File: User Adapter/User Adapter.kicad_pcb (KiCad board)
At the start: 2 copper layers, 88.9 x 27.9 mm, 20 parts, among them J1 OHIS_8p8c_Shield, J2 Headphones, J3 Microphone, J4 PTT, J5 Dynamic Mic Bypass, J6 HP or CTIA, Q1 2N3904, SW1 SW_Push

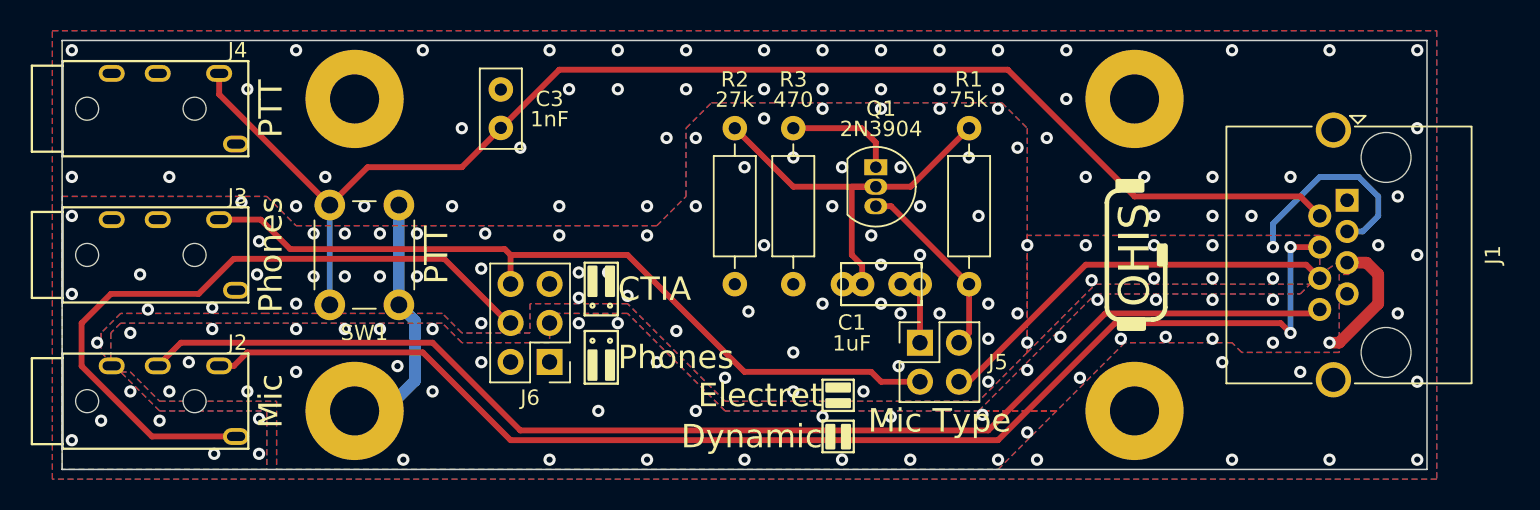
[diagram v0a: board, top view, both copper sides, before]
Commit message: https://github.com/open-headset-interconnect-standard/ohis/issues/14 v1.0a as ordered 2023-10-05.
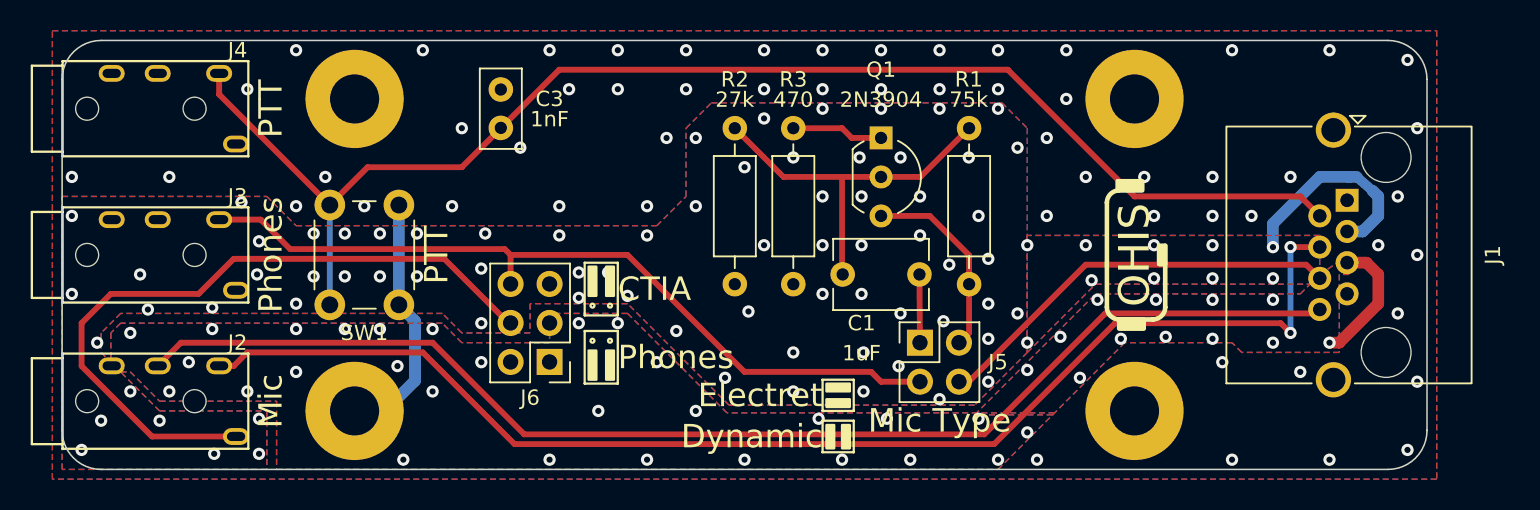
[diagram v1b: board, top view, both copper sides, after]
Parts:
- removed C2: 1uF, Capacitor_THT:C_Disc_D5.0mm_W2.5mm_P5.00mm
- added BOM1: .1" Jumper, Libraries:BOM_Item, F.Cu at (196.3, 67.4)
- added BOM10: M3 6mm SS screw, Libraries:BOM_Item, F.Cu at (196.0, 88.4)
- added BOM11: M3 6mm SS screw, Libraries:BOM_Item, F.Cu at (197.5, 85.4)
- added BOM12: M3 6mm SS screw, Libraries:BOM_Item, F.Cu at (197.5, 86.9)
- added BOM13: M3 10mm SS screw, Libraries:BOM_Item, F.Cu at (197.5, 88.4)
- added BOM14: M3 10mm SS screw, Libraries:BOM_Item, F.Cu at (194.1, 89.7)
- added BOM15: M3 10mm SS screw, Libraries:BOM_Item, F.Cu at (194.1, 91.2)
- added BOM16: M3 10mm SS screw, Libraries:BOM_Item, F.Cu at (195.6, 89.7)
- added BOM17: Main Board, Libraries:BOM_Item, F.Cu at (195.3, 79.5)
- added BOM18: Top Board, Libraries:BOM_Item, F.Cu at (195.3, 81.0)
- added BOM19: Bottom Board, Libraries:BOM_Item, F.Cu at (195.6, 91.2)
- added BOM2: .1" Jumper, Libraries:BOM_Item, F.Cu at (196.3, 68.9)
- added BOM20: M3 3mm ABS standoff, Libraries:BOM_Item, F.Cu at (197.1, 89.7)
- added BOM21: M3 3mm ABS standoff, Libraries:BOM_Item, F.Cu at (197.1, 91.2)
- added BOM22: M3 3mm ABS standoff, Libraries:BOM_Item, F.Cu at (198.6, 89.7)
- added BOM23: M3 3mm ABS standoff, Libraries:BOM_Item, F.Cu at (198.6, 91.2)
- added BOM3: .1" Jumper, Libraries:BOM_Item, F.Cu at (196.3, 70.4)
- added BOM4: .1" Jumper, Libraries:BOM_Item, F.Cu at (196.3, 71.9)
- added BOM5: M3 14mm brass standoff, Libraries:BOM_Item, F.Cu at (194.5, 85.4)
- added BOM6: M3 14mm brass standoff, Libraries:BOM_Item, F.Cu at (194.5, 86.9)
- added BOM7: M3 14mm brass standoff, Libraries:BOM_Item, F.Cu at (194.5, 88.4)
- added BOM8: M3 14mm brass standoff, Libraries:BOM_Item, F.Cu at (196.0, 85.4)
- added BOM9: M3 6mm SS screw, Libraries:BOM_Item, F.Cu at (196.0, 86.9)
- C1: footprint Capacitor_THT:C_Disc_D5.0mm_W2.5mm_P2.50mm -> Capacitor_THT:C_Disc_D6.0mm_W4.4mm_P5.00mm
- Q1: footprint Package_TO_SOT_THT:TO-92_Inline -> Package_TO_SOT_THT:TO-92_Inline_Wide
- SW1: value SW_Push -> PTT
- moved Q1 1.94 mm to (154.9, 68.6)
- moved C1 1.38 mm to (157.4, 77.5)
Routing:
- net Net-(Q1-B): track 27.9 -> 24.9 mm
- net Net-(Q1-E): track 7.37 -> 5.98 mm
- net Net-(J5-Pin_2): track 12.3 -> 12.8 mm
- net Mic-: vias 79 -> 84
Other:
- outline, holes or cut-outs redrawn

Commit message: Fixed silkscreen art, added trimpot. #1
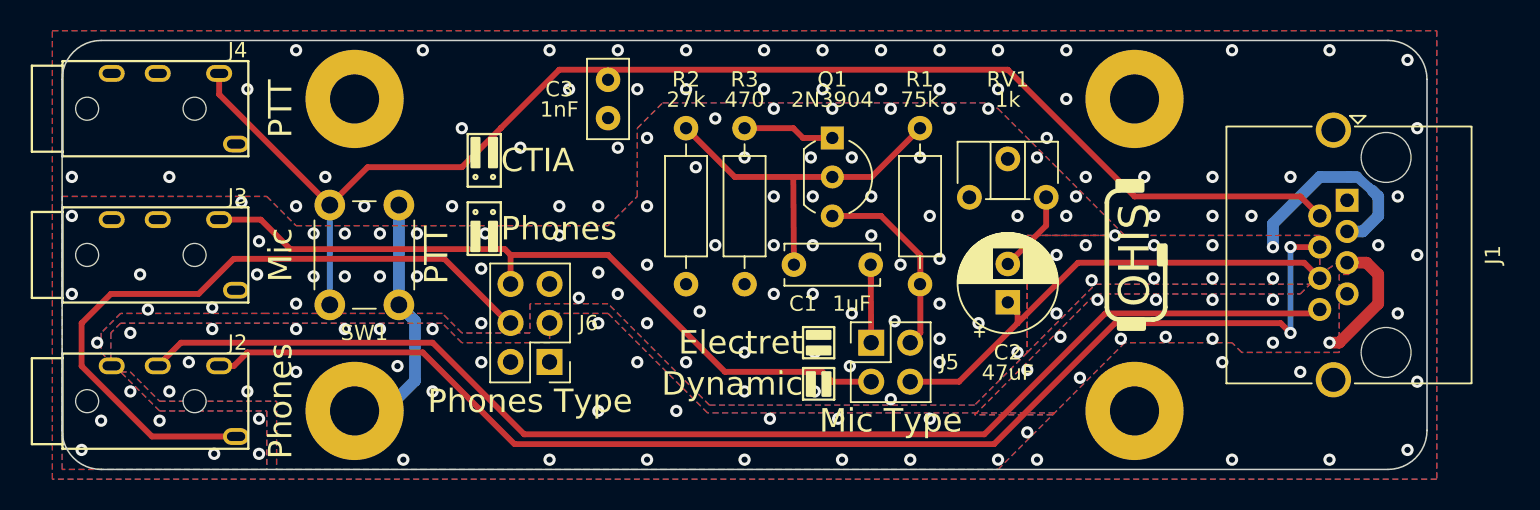
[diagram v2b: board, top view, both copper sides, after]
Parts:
- added C2: 47uF, Capacitor_THT:CP_Radial_D6.3mm_P2.50mm, F.Cu at (163.2, 79.3)
- added RV1: 1k, Potentiometer_THT:Potentiometer_Piher_PT-6-H_Horizontal, F.Cu at (160.7, 72.4)
- C1: footprint Capacitor_THT:C_Disc_D6.0mm_W4.4mm_P5.00mm -> Capacitor_THT:C_Disc_D6.0mm_W2.5mm_P5.00mm
- moved C3 7.23 mm to (137.2, 67.3), turned to 90 degrees
- moved C1 3.24 mm to (154.3, 76.8)
- moved R1 3.20 mm to (157.5, 78.1)
- moved Q1 3.18 mm to (151.8, 68.6)
- moved J5 3.17 mm to (154.3, 81.9)
- moved R2 3.17 mm to (142.2, 67.9)
- moved R3 3.17 mm to (146.1, 67.9)
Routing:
- net Net-(C2-Pad2): track 0.00 -> 5.38 mm
- net Mic+: track 27.0 -> 31.9 mm
- net Mic+ 3.5: track 51.9 -> 48.7 mm
- net Net-(Q1-B): track 24.9 -> 23.6 mm
- net Net-(J5-Pin_1): track 5.08 -> 6.35 mm
- net Mic-: vias 84 -> 91
- net HP:G: vias 41 -> 40
- net GND: vias 56 -> 55
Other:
- board text added: "1k"
- board text added: "47uF"
- board text added: "JLCJLCJLCJLC"
- board text added: "OHIS Open Source User Adapter v1.1a 2024 CC-BY OHIS Working Group"
- board text added: "Phones Type"
- board text removed: "OHIS Open Source User Adapter 2023 CC-BY OHIS Working Group"

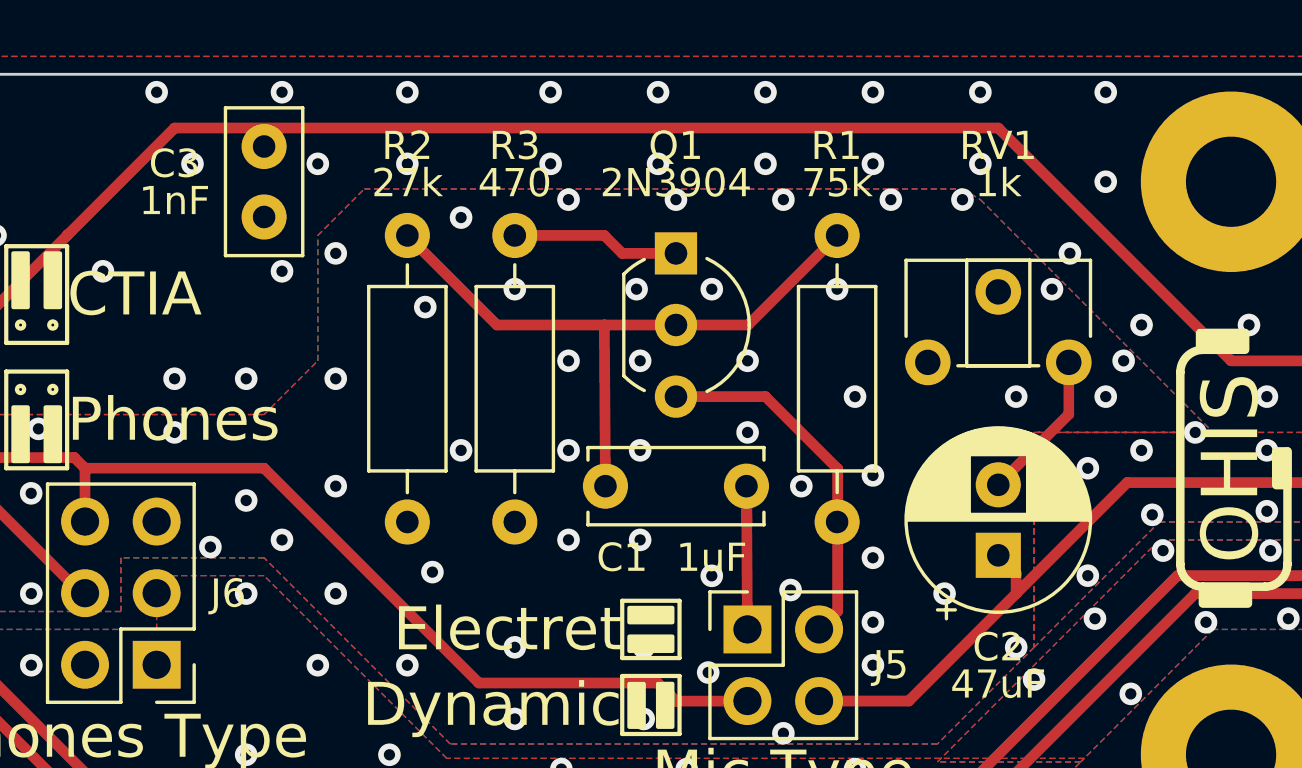
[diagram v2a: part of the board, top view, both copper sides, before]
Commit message: Very minor changes to the silkscreen when ordering. AS ORDERED prototypes v1.1
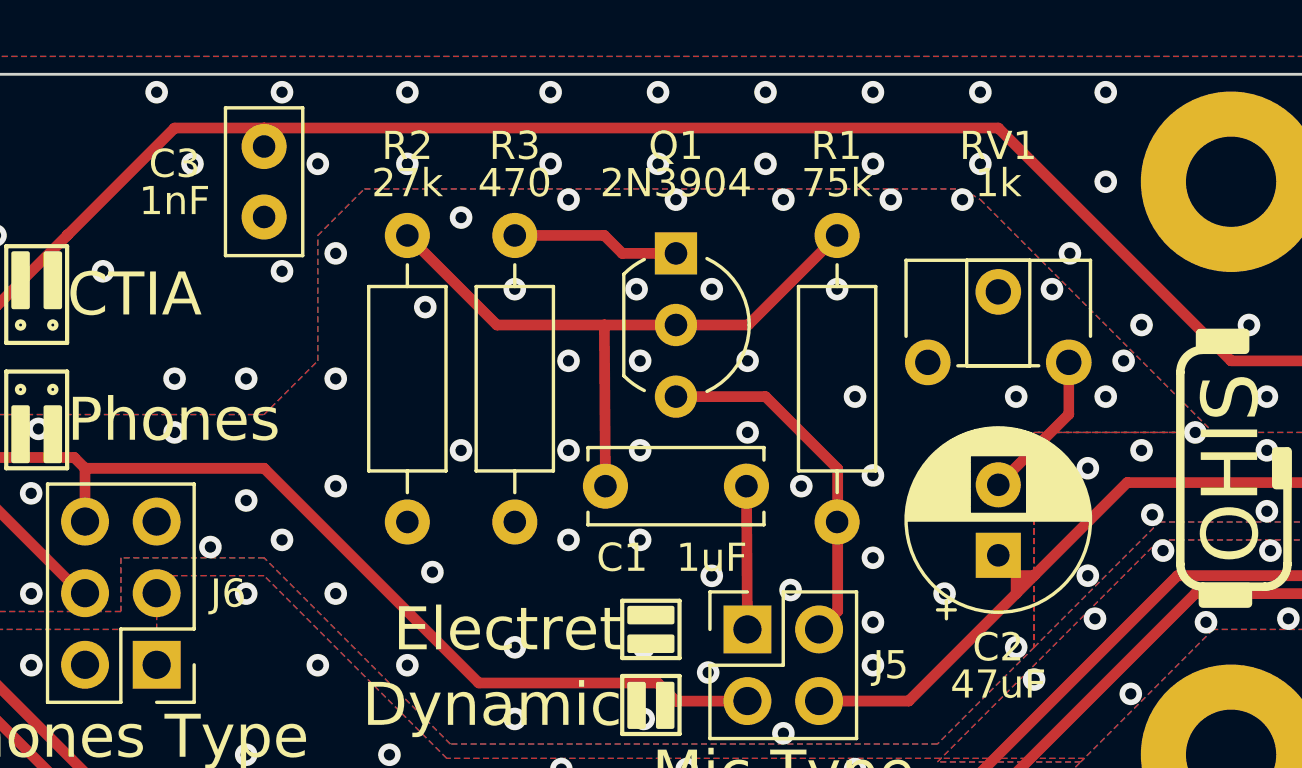
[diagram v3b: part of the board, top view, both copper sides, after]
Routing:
- net Mic+: track 31.9 -> 33.5 mm
- net Net-(J5-Pin_1): track 6.35 -> 5.08 mm
- net PTT: track 90.1 -> 90.8 mm
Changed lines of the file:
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@@
     (effects (font (size 1.27 1.27) (thickness 0.1905)) (justify left mirror))
   )
-  (gr_text "OHIS Open Source User Adapter v1.1a\n2024 CC-BY OHIS Working Group" (at 166.37 66.675) (layer "B.SilkS")
-    (effects (font (size 1.27 1.27) (thickness 0.1905)) (justify left bottom mirror))
-  )
-  (gr_text "https://github.com/open-headset-interconnect-standard/user-adapter" (at 180.34 76.581) (layer "B.SilkS")
+  (gr_text "OHIS Open Source User Adapter v1.1a\n2024 CC-BY OHIS Working Group" (at 167.64 66.675) (layer "B.SilkS")
+    (effects (font (size 1.27 1.016) (thickness 0.1905)) (justify left bottom mirror))
+  )
+  (gr_text "https://github.com/open-headset-interconnect-standard/user-adapter" (at 180.34 75.819) (layer "B.SilkS")
     (effects (font (size 1 1) (thickness 0.15)) (justify left bottom mirror))
   )
@@
   (segment (start 171.45 72.39) (end 182.249 72.39) (width 0.381) (layer "F.Cu") (net 3))
   (segment (start 111.83 65.745) (end 119.035 72.95) (width 0.381) (layer "F.Cu") (net 3))
-  (segment (start 133.985 64.135) (end 163.195 64.135) (width 0.381) (layer "F.Cu") (net 3))
+  (segment (start 137.16 64.135) (end 163.195 64.135) (width 0.381) (layer "F.Cu") (net 3))
   (segment (start 182.249 72.39) (end 183.515 73.656) (width 0.381) (layer "F.Cu") (net 3))
   (segment (start 130.175 67.925) (end 130.195 67.925) (width 0.381) (layer "F.Cu") (net 3))
   (segment (start 121.5 70.485) (end 127.635 70.485) (width 0.381) (layer "F.Cu") (net 3))
   (segment (start 111.83 64.375) (end 111.83 65.745) (width 0.381) (layer "F.Cu") (net 3))
+  (segment (start 133.985 64.135) (end 137.16 64.135) (width 0.381) (layer "F.Cu") (net 3))
   (segment (start 130.195 67.925) (end 133.985 64.135) (width 0.381) (layer "F.Cu") (net 3))
+  (segment (start 137.16 64.79) (end 137.16 64.135) (width 0.381) (layer "F.Cu") (net 3))
   (segment (start 163.195 64.135) (end 171.45 72.39) (width 0.381) (layer "F.Cu") (net 3))
   (segment (start 119.035 79.45) (end 119.035 72.95) (width 0.381) (layer "B.Cu") (net 3))
@@
   (via (at 108.585 85.09) (size 0.8) (drill 0.4) (layers "F.Cu" "B.Cu") (free) (net 6))
   (via (at 172.847 79.121) (size 0.8) (drill 0.4) (layers "F.Cu" "B.Cu") (free) (net 6))
+  (segment (start 163.195 79.28738) (end 163.91762 80.01) (width 0.381) (layer "F.Cu") (net 7))
+  (segment (start 163.83 80.645) (end 164.465 80.01) (width 0.381) (layer "F.Cu") (net 7))
   (segment (start 163.83 80.645) (end 163.83 79.92238) (width 0.381) (layer "F.Cu") (net 7))
   (segment (start 160.02 84.455) (end 163.83 80.645) (width 0.381) (layer "F.Cu") (net 7))
-  (segment (start 163.83 80.645) (end 167.767 76.708) (width 0.381) (layer "F.Cu") (net 7))
+  (segment (start 164.465 80.01) (end 167.767 76.708) (width 0.381) (layer "F.Cu") (net 7))
+  (segment (start 163.91762 80.01) (end 164.465 80.01) (width 0.381) (layer "F.Cu") (net 7))
   (segment (start 156.84 84.455) (end 160.02 84.455) (width 0.381) (layer "F.Cu") (net 7))
   (segment (start 167.767 76.708) (end 182.503 76.708) (width 0.381) (layer "F.Cu") (net 7))
@@
   (segment (start 104.775 78.74) (end 102.87 80.645) (width 0.381) (layer "F.Cu") (net 12))
   (segment (start 107.456 88.025) (end 112.93 88.025) (width 0.381) (layer "F.Cu") (net 12))
-  (segment (start 154.265 76.835) (end 154.285 78.105) (width 0.381) (layer "F.Cu") (net 13))
   (segment (start 154.3 81.915) (end 154.265 76.835) (width 0.381) (layer "F.Cu") (net 13))
   (segment (start 154.94 73.66) (end 157.5 76.22) (width 0.381) (layer "F.Cu") (net 14))

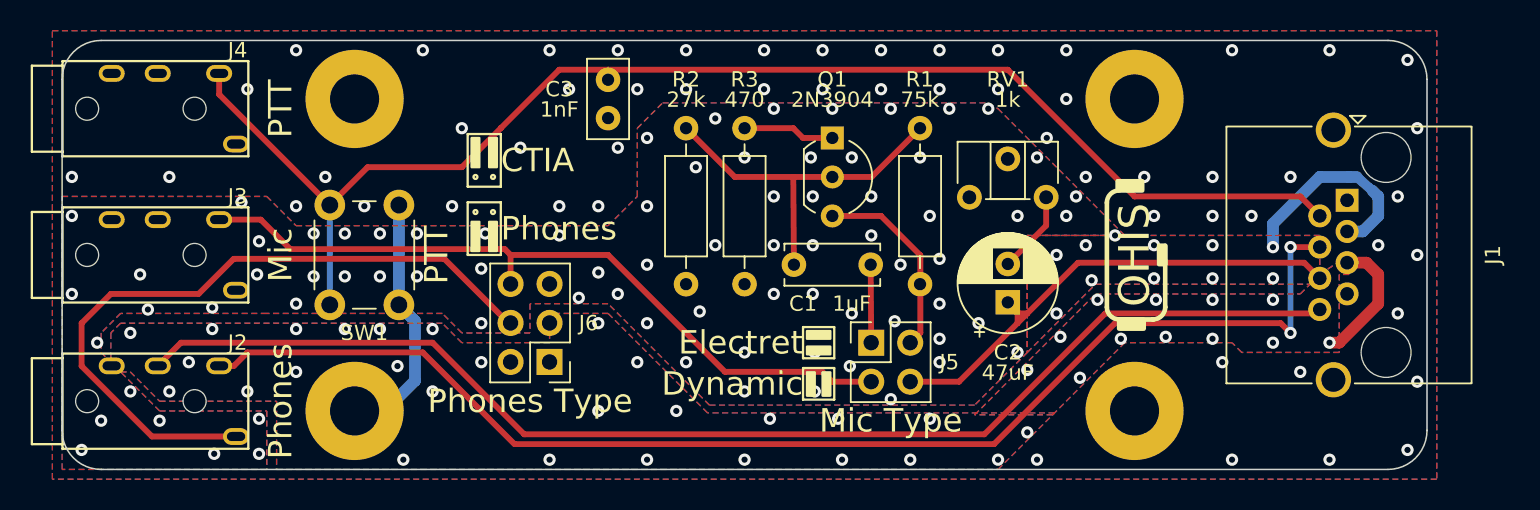
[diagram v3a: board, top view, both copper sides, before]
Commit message: Cleaned up board, moved jumpers to right-angle at board edge.
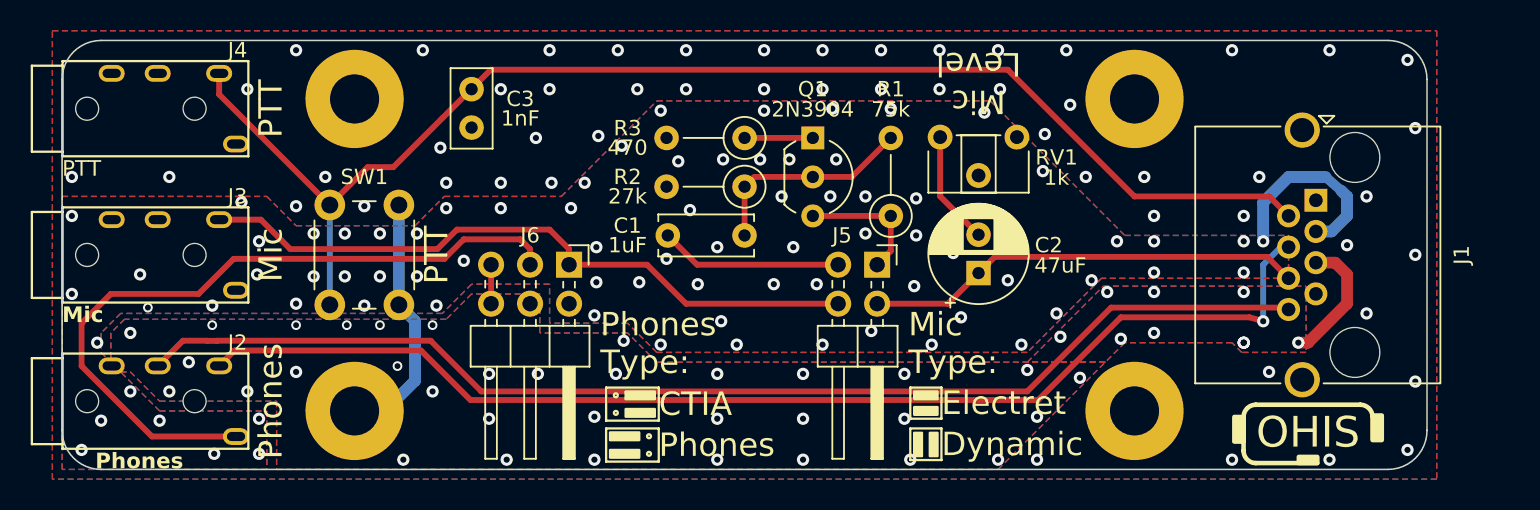
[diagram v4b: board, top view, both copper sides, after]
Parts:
- J5: footprint Connector_PinHeader_2.54mm:PinHeader_2x02_P2.54mm_Vertical -> Connector_PinHeader_2.54mm:PinHeader_2x02_P2.54mm_Horizontal
- J6: footprint Connector_PinHeader_2.54mm:PinHeader_2x03_P2.54mm_Vertical -> Connector_PinHeader_2.54mm:PinHeader_2x03_P2.54mm_Horizontal
- R1, R2, R3: footprint Resistor_THT:R_Axial_DIN0207_L6.3mm_D2.5mm_P10.16mm_Horizontal -> Resistor_THT:R_Axial_DIN0207_L6.3mm_D2.5mm_P5.08mm_Vertical
- moved G1 16.2 mm to (182.8, 87.8), turned to 0 degrees
- moved C1 13.4 mm to (141.1, 74.9), turned to 0 degrees
- moved G*** 12.7 mm to (132.1, 85.1)
- moved C3 8.91 mm to (128.3, 67.9)
- moved J6 6.46 mm to (134.6, 76.8), turned to -90 degrees
- moved R2 5.39 mm to (146.1, 71.8), turned to 180 degrees
- moved J5 5.09 mm to (154.7, 76.8), turned to -90 degrees
- moved RV1 4.99 mm to (163.8, 68.5), turned to -90 degrees
- moved R1 4.84 mm to (155.6, 73.7)
- moved C2 2.69 mm to (161.3, 77.4)
- moved J1 2.03 mm to (183.3, 72.6)
- moved Q1 1.27 mm to (150.5, 68.6)
- moved R3 0.64 mm to (146.1, 68.6), turned to 180 degrees
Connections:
- C1 pad 1: Net-(J5-Pin_1) -> Net-(J5-Pin_3)
- J2 pad S: Net-(J6-Pin_4) -> Net-(J6-Pin_3)
- J5 pad 2: Net-(J5-Pin_2) -> Mic+
- J5 pad 3: Mic+ 3.5 -> Net-(J5-Pin_3)
- J5 pad 4: Mic+ -> Mic+ 3.5
- J6 pad 1: HP:G -> Mic+ 3.5
- J6 pad 2: HP:G -> Mic-
- J6 pad 3: HP:G -> Net-(J6-Pin_3)
- J6 pad 4: Net-(J6-Pin_4) -> HP:G
- J6 pad 5: Mic- -> HP:G
- J6 pad 6: Mic+ 3.5 -> HP:G
- Q1 pad 3: Net-(J5-Pin_2) -> Net-(J5-Pin_1)
- R1 pad 1: Net-(J5-Pin_2) -> Net-(J5-Pin_1)
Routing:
- net Net-(J6-Pin_3): track 0.00 -> 47.5 mm
- net Net-(J6-Pin_4): track 46.2 -> 0.00 mm
- net Net-(J5-Pin_2): track 12.8 -> 0.00 mm
- net Net-(J5-Pin_3): track 0.00 -> 11.9 mm
- net Net-(Q1-B): track 23.6 -> 14.0 mm
- net HP:L: track 83.6 -> 77.8 mm, vias 2 -> 1
- net Mic+: track 33.5 -> 28.6 mm
- net Mic+ 3.5: track 48.7 -> 44.2 mm
- net HP:R: track 82.2 -> 78.0 mm
- net Net-(J5-Pin_1): track 5.08 -> 8.62 mm
- net PTT: track 90.8 -> 88.1 mm
- net HP:G: track 8.48 -> 11.0 mm, vias 40 -> 43
- net Net-(C2-Pad2): track 5.38 -> 7.39 mm
- net Net-(Q1-E): track 5.98 -> 4.44 mm
- net Mic-: track 13.9 -> 12.9 mm, vias 91 -> 81
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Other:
- board text added: "Mic Level"
- board text added: "Mic Type:"
- board text added: "OHIS User Adapter v1.2a 2024 CC-BY OHIS Working Group"
- board text added: "Phones Type:"
- board text added: "https://ohis.org/hardware/"
- board text removed: "Mic Type"
- board text removed: "OHIS Open Source User Adapter v1.1a 2024 CC-BY OHIS Working Group"
- board text removed: "Phones Type"
- board text removed: "https://github.com/open-headset-interconnect-standard/user-adapter"
